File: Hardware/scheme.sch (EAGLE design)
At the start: 9 parts, among them IC1 74HC14N, IC2 LTC485N

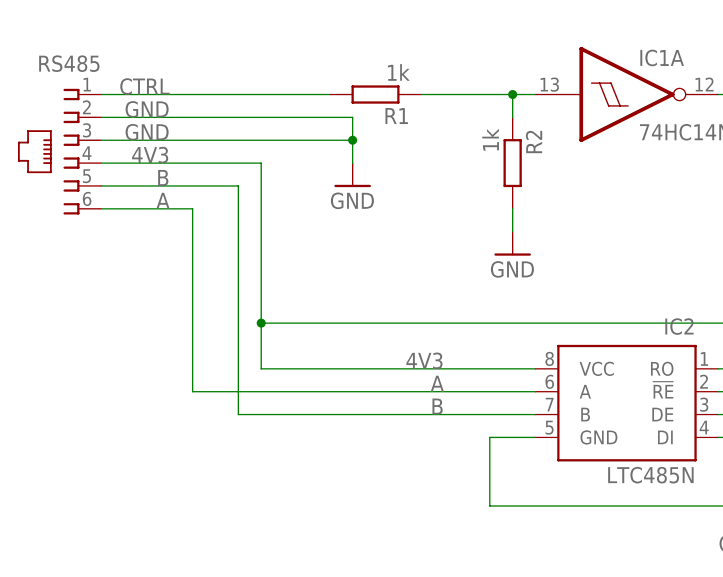
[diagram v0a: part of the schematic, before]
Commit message: Add 120 Ohm resistor between A and B
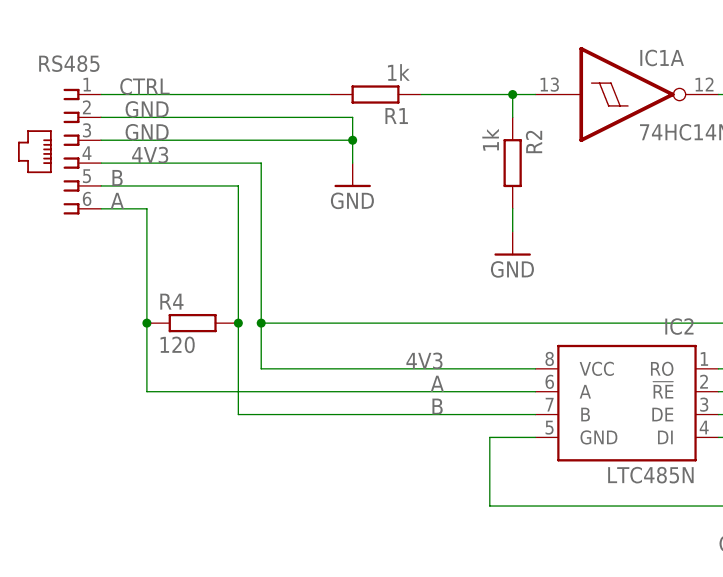
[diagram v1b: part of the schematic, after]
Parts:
- added R4: 120, rcl:R-EU_0204/7
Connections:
- net A: now also R4.1
- net B: now also R4.2
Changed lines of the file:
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@@
 <part name="GND3" library="supply1" deviceset="GND" device=""/>
 <part name="GND4" library="supply1" deviceset="GND" device=""/>
+<part name="R4" library="rcl" deviceset="R-EU_" device="0204/7" value="120"/>
 </parts>
 <sheets>
@@
 <instance part="GND3" gate="1" x="-15.24" y="50.8"/>
 <instance part="GND4" gate="1" x="60.96" y="60.96"/>
+<instance part="R4" gate="G$1" x="-33.02" y="35.56"/>
 </instances>
 <busses>
@@
 <net name="A" class="0">
 <segment>
-<pinref part="RS485" gate="G$1" pin="6"/>
-<wire x1="-33.02" y1="48.26" x2="-43.18" y2="48.26" width="0.1524" layer="91"/>
-<label x="-35.56" y="48.26" size="1.778" layer="95" rot="MR0"/>
-<wire x1="-33.02" y1="48.26" x2="-33.02" y2="27.94" width="0.1524" layer="91"/>
 <pinref part="IC2" gate="G$1" pin="A"/>
 <label x="-5.08" y="27.94" size="1.778" layer="95" rot="MR0"/>
-<wire x1="-33.02" y1="27.94" x2="5.08" y2="27.94" width="0.1524" layer="91"/>
+<wire x1="-38.1" y1="27.94" x2="5.08" y2="27.94" width="0.1524" layer="91"/>
+<pinref part="R4" gate="G$1" pin="1"/>
+<pinref part="RS485" gate="G$1" pin="6"/>
+<wire x1="-43.18" y1="48.26" x2="-38.1" y2="48.26" width="0.1524" layer="91"/>
+<wire x1="-38.1" y1="48.26" x2="-38.1" y2="35.56" width="0.1524" layer="91"/>
+<label x="-40.64" y="48.26" size="1.778" layer="95" rot="MR0"/>
+<wire x1="-38.1" y1="27.94" x2="-38.1" y2="35.56" width="0.1524" layer="91"/>
+<junction x="-38.1" y="35.56"/>
 </segment>
 </net>
@@
 <pinref part="RS485" gate="G$1" pin="5"/>
 <wire x1="-43.18" y1="50.8" x2="-27.94" y2="50.8" width="0.1524" layer="91"/>
-<label x="-35.56" y="50.8" size="1.778" layer="95" rot="MR0"/>
-<wire x1="-27.94" y1="50.8" x2="-27.94" y2="25.4" width="0.1524" layer="91"/>
+<label x="-40.64" y="50.8" size="1.778" layer="95" rot="MR0"/>
+<wire x1="-27.94" y1="50.8" x2="-27.94" y2="35.56" width="0.1524" layer="91"/>
 <pinref part="IC2" gate="G$1" pin="B"/>
+<wire x1="-27.94" y1="35.56" x2="-27.94" y2="25.4" width="0.1524" layer="91"/>
 <wire x1="5.08" y1="25.4" x2="-27.94" y2="25.4" width="0.1524" layer="91"/>
 <label x="-5.08" y="25.4" size="1.778" layer="95" rot="MR0"/>
+<pinref part="R4" gate="G$1" pin="2"/>
+<junction x="-27.94" y="35.56"/>
 </segment>
 </net>

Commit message: Minor fixes and additional comments
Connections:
- removed net GND1: C1.1, C2.1, IC1P.GND
- net GND: now also C1.1, C2.1, IC1P.GND
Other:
- moved on the sheet: C1, C2, IC1P
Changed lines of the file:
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@@
 <part name="GND4" library="supply1" deviceset="GND" device=""/>
 <part name="R4" library="rcl" deviceset="R-EU_" device="0204/7" value="120"/>
+<part name="GND5" library="supply1" deviceset="GND" device=""/>
 </parts>
 <sheets>
@@
 <instance part="RS485" gate="G$1" x="-45.72" y="55.88" rot="MR0"/>
 <instance part="IC1" gate="A" x="15.24" y="60.96"/>
-<instance part="IC1" gate="P" x="12.7" y="-27.94" rot="R90"/>
-<instance part="C1" gate="G$1" x="15.24" y="-33.02" rot="R270"/>
+<instance part="IC1" gate="P" x="111.76" y="43.18"/>
+<instance part="C1" gate="G$1" x="106.68" y="40.64" rot="R180"/>
 <instance part="R1" gate="G$1" x="-12.7" y="60.96" rot="R180"/>
 <instance part="R2" gate="G$1" x="2.54" y="53.34" rot="R270"/>
 <instance part="GND1" gate="1" x="2.54" y="43.18"/>
 <instance part="IC2" gate="G$1" x="15.24" y="27.94" rot="MR0"/>
-<instance part="C2" gate="G$1" x="15.24" y="-38.1" rot="R270"/>
+<instance part="C2" gate="G$1" x="93.98" y="40.64" rot="R180"/>
 <instance part="R3" gate="G$1" x="58.42" y="25.4" rot="R270"/>
 <instance part="GND2" gate="1" x="27.94" y="12.7"/>
@@
 <instance part="GND4" gate="1" x="60.96" y="60.96"/>
 <instance part="R4" gate="G$1" x="-33.02" y="35.56"/>
+<instance part="GND5" gate="1" x="111.76" y="12.7"/>
 </instances>
 <busses>
@@
 <pinref part="GND2" gate="1" pin="GND"/>
 <junction x="27.94" y="15.24"/>
+</segment>
+<segment>
+<pinref part="C2" gate="G$1" pin="1"/>
+<wire x1="93.98" y1="38.1" x2="93.98" y2="27.94" width="0.1524" layer="91"/>
+<pinref part="IC1" gate="P" pin="GND"/>
+<wire x1="111.76" y1="35.56" x2="111.76" y2="27.94" width="0.1524" layer="91"/>
+<pinref part="C1" gate="G$1" pin="1"/>
+<wire x1="111.76" y1="27.94" x2="111.76" y2="15.24" width="0.1524" layer="91"/>
+<wire x1="106.68" y1="38.1" x2="106.68" y2="27.94" width="0.1524" layer="91"/>
+<wire x1="106.68" y1="27.94" x2="111.76" y2="27.94" width="0.1524" layer="91"/>
+<junction x="111.76" y="27.94"/>
+<wire x1="93.98" y1="27.94" x2="106.68" y2="27.94" width="0.1524" layer="91"/>
+<junction x="106.68" y="27.94"/>
+<pinref part="GND5" gate="1" pin="GND"/>
 </segment>
 </net>
@@
 <segment>
 <pinref part="C2" gate="G$1" pin="2"/>
-<wire x1="10.16" y1="-38.1" x2="-2.54" y2="-38.1" width="0.1524" layer="91"/>
+<wire x1="93.98" y1="45.72" x2="93.98" y2="58.42" width="0.1524" layer="91"/>
 <pinref part="IC1" gate="P" pin="VCC"/>
-<wire x1="5.08" y1="-27.94" x2="-2.54" y2="-27.94" width="0.1524" layer="91"/>
-<label x="-12.7" y="-27.94" size="1.778" layer="95"/>
+<wire x1="111.76" y1="50.8" x2="111.76" y2="58.42" width="0.1524" layer="91"/>
 <pinref part="C1" gate="G$1" pin="2"/>
-<wire x1="-2.54" y1="-27.94" x2="-12.7" y2="-27.94" width="0.1524" layer="91"/>
-<wire x1="10.16" y1="-33.02" x2="-2.54" y2="-33.02" width="0.1524" layer="91"/>
-<wire x1="-2.54" y1="-33.02" x2="-2.54" y2="-27.94" width="0.1524" layer="91"/>
-<junction x="-2.54" y="-27.94"/>
-<wire x1="-2.54" y1="-38.1" x2="-2.54" y2="-33.02" width="0.1524" layer="91"/>
-<junction x="-2.54" y="-33.02"/>
+<wire x1="111.76" y1="58.42" x2="111.76" y2="68.58" width="0.1524" layer="91"/>
+<wire x1="106.68" y1="45.72" x2="106.68" y2="58.42" width="0.1524" layer="91"/>
+<wire x1="106.68" y1="58.42" x2="111.76" y2="58.42" width="0.1524" layer="91"/>
+<junction x="111.76" y="58.42"/>
+<wire x1="93.98" y1="58.42" x2="106.68" y2="58.42" width="0.1524" layer="91"/>
+<junction x="106.68" y="58.42"/>
+<label x="109.22" y="68.58" size="1.778" layer="95"/>
 </segment>
 </net>
@@
 </segment>
 </net>
-<net name="GND1" class="0">
-<segment>
-<pinref part="C2" gate="G$1" pin="1"/>
-<wire x1="17.78" y1="-38.1" x2="27.94" y2="-38.1" width="0.1524" layer="91"/>
-<pinref part="IC1" gate="P" pin="GND"/>
-<wire x1="20.32" y1="-27.94" x2="27.94" y2="-27.94" width="0.1524" layer="91"/>
-<label x="35.56" y="-27.94" size="1.778" layer="95"/>
-<pinref part="C1" gate="G$1" pin="1"/>
-<wire x1="27.94" y1="-27.94" x2="40.64" y2="-27.94" width="0.1524" layer="91"/>
-<wire x1="17.78" y1="-33.02" x2="27.94" y2="-33.02" width="0.1524" layer="91"/>
-<wire x1="27.94" y1="-33.02" x2="27.94" y2="-27.94" width="0.1524" layer="91"/>
-<junction x="27.94" y="-27.94"/>
-<wire x1="27.94" y1="-38.1" x2="27.94" y2="-33.02" width="0.1524" layer="91"/>
-<junction x="27.94" y="-33.02"/>
-</segment>
-</net>
